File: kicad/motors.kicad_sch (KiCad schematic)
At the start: 33 parts, among them U1 DRV8251A, U15 DRV8251A, U16 DRV8251A, U17 DRV8251A, U2 DRV8251A, U3 DRV8251A

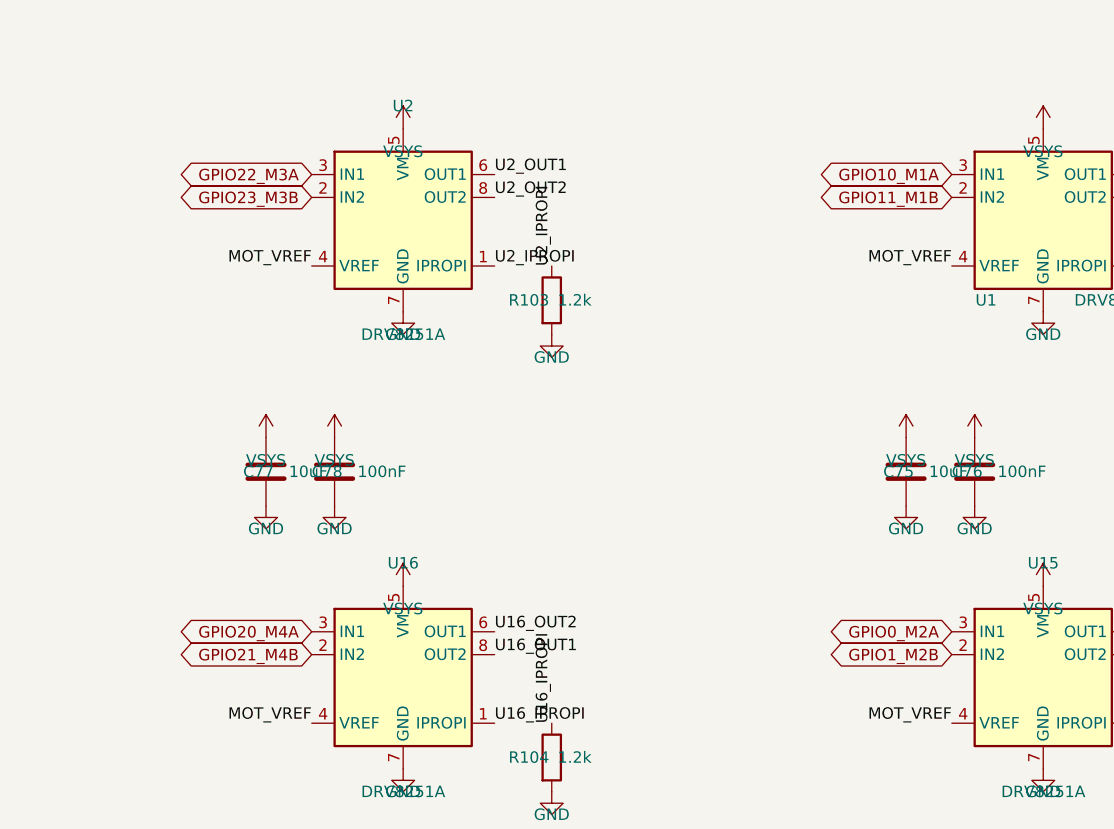
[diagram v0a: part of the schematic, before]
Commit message: Rotate U10 to 0 deg and re-place the brain at 66.6 x 32 mm, unrouted
USB now runs straight down from J1 into U10's north pins; IO goes west to J5,
which moves to the top of the left wall with M5/M6 below it. SW1 sits under
U16 and SW2 in the bottom-right corner; Q1 is east of J3. GPIO map redone for
the new orientation (IO1-6 on GPIO0-3/8/9, motors on GPIO12-17/20-23/26-27,
USB-A on GPIO24/25, LED on GPIO29). ERC clean, DRC parity clean.

Co-Authored-By: Claude Opus 5.5 <noreply@anthropic.com>
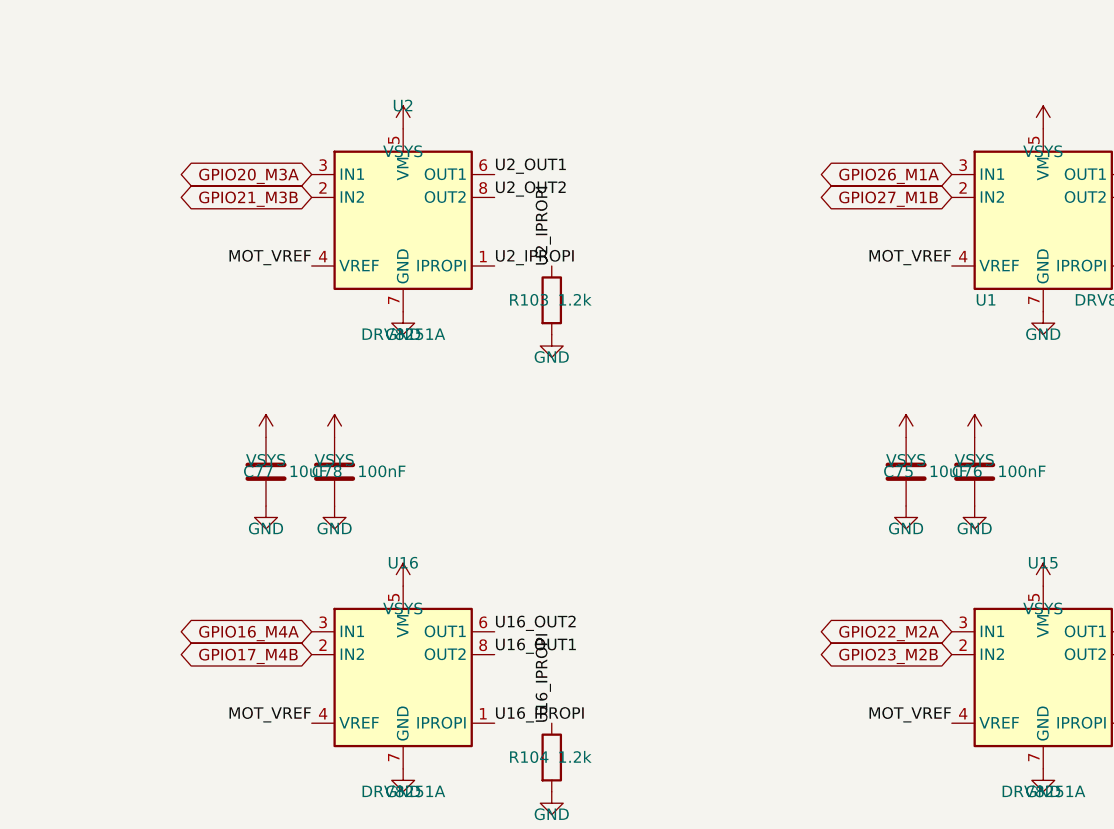
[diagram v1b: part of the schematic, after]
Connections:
- net GPIO0_M2A renamed GPIO22_M2A
- net GPIO10_M1A renamed GPIO26_M1A
- net GPIO11_M1B renamed GPIO27_M1B
- net GPIO1_M2B renamed GPIO23_M2B
- net GPIO20_M4A renamed GPIO16_M4A
- net GPIO21_M4B renamed GPIO17_M4B
- net GPIO22_M3A renamed GPIO20_M3A
- net GPIO23_M3B renamed GPIO21_M3B
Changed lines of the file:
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@@
 		)
 	)
-	(global_label "GPIO10_M1A"
+	(global_label "GPIO26_M1A"
 		(shape bidirectional)
 		(at 205.74 83.82 180)
@@
 		)
 	)
-	(global_label "GPIO1_M2B"
+	(global_label "GPIO23_M2B"
 		(shape bidirectional)
 		(at 205.74 137.16 180)
@@
 		)
 	)
-	(global_label "GPIO23_M3B"
+	(global_label "GPIO21_M3B"
 		(shape bidirectional)
 		(at 134.62 86.36 180)
@@
 		)
 	)
-	(global_label "GPIO0_M2A"
+	(global_label "GPIO22_M2A"
 		(shape bidirectional)
 		(at 205.74 134.62 180)
@@
 		)
 	)
-	(global_label "GPIO20_M4A"
+	(global_label "GPIO16_M4A"
 		(shape bidirectional)
 		(at 134.62 134.62 180)
@@
 		)
 	)
-	(global_label "GPIO22_M3A"
+	(global_label "GPIO20_M3A"
 		(shape bidirectional)
 		(at 134.62 83.82 180)
@@
 		)
 	)
-	(global_label "GPIO11_M1B"
+	(global_label "GPIO27_M1B"
 		(shape bidirectional)
 		(at 205.74 86.36 180)
@@
 		)
 	)
-	(global_label "GPIO21_M4B"
+	(global_label "GPIO17_M4B"
 		(shape bidirectional)
 		(at 134.62 137.16 180)
